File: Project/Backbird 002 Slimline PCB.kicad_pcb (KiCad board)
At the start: 2 copper layers, 10 parts

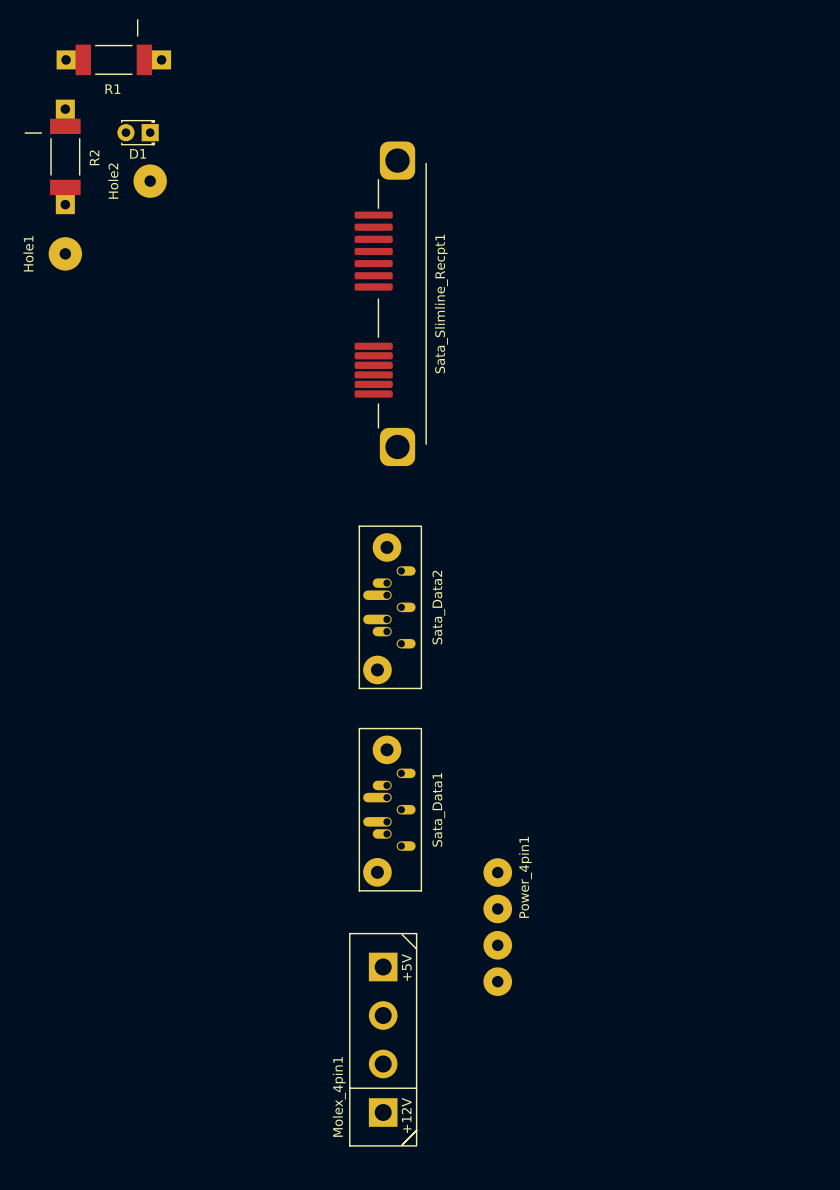
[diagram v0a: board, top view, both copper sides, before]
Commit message: Updated PSB layout. (might remove extra power and Sata locations) Added custom footprints for screws and for a generic 8981 power pinout.
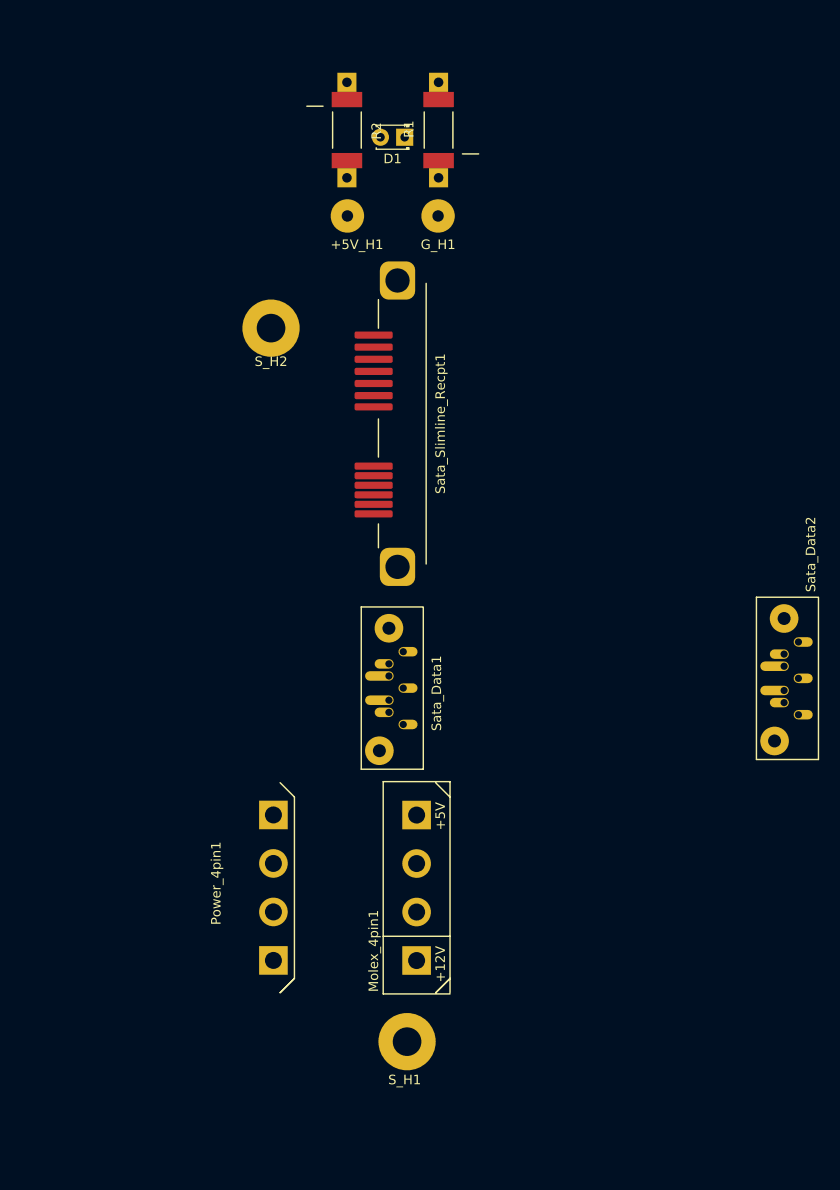
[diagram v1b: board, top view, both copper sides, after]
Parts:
- removed Hole1, Hole2: Conn_01x01, Wire_Pads:SolderWirePad_single_1-2mmDrill
- added +5V_H1: Conn_01x01, Wire_Pads:SolderWirePad_single_1-2mmDrill, F.Cu at (102.5, 46.5)
- added G_H1: Conn_01x01, Wire_Pads:SolderWirePad_single_1-2mmDrill, F.Cu at (112.0, 46.5)
- added S_H1: Conn_01x01, ProjectFootprints:Blackbird002_Slimline_PCB_Screw, F.Cu at (108.8, 133.0)
- added S_H2: Conn_01x01, ProjectFootprints:Blackbird002_Slimline_PCB_Screw, F.Cu at (94.5, 58.2)
- Power_4pin1: footprint Wire_Pads:SolderWirePad_4xInline_1-2mmDrill -> ProjectFootprints:MOLEX_8981_Generic
- moved Sata_Data2 42.3 mm to (152.7, 103.3)
- moved R1 34.8 mm to (112.1, 37.5), turned to 90 degrees
- moved R2 29.6 mm to (102.5, 37.5)
- moved D1 26.7 mm to (108.5, 38.2)
- moved Power_4pin1 23.9 mm to (94.8, 116.8)
- moved Molex_4pin1 16.3 mm to (109.8, 116.9)
- moved Sata_Data1 12.7 mm to (111.3, 104.3)
- moved Sata_Slimline_Recpt1 12.6 mm to (107.8, 68.2)

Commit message: Removed extra connectors from PCB
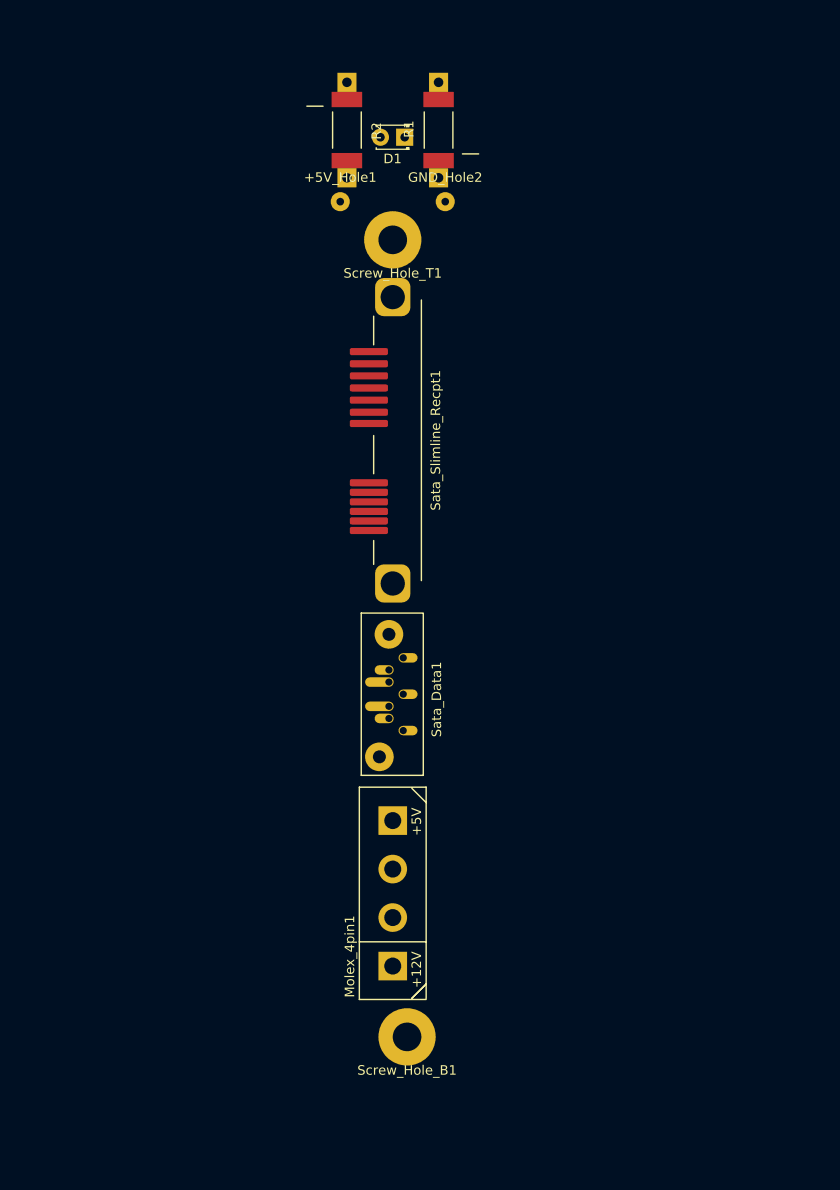
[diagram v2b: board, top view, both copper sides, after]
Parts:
- removed +5V_H1, G_H1: Conn_01x01, Wire_Pads:SolderWirePad_single_1-2mmDrill
- removed Power_4pin1: Conn_01x04, ProjectFootprints:MOLEX_8981_Generic
- removed S_H1, S_H2: Conn_01x01, ProjectFootprints:Blackbird002_Slimline_PCB_Screw
- removed Sata_Data2: Conn_01x07, ProjectFootprints:SATA_DATA_678007005_CustomPad
- added +5V_Hole1: Conn_01x01, Wire_Pads:SolderWirePad_single_0-8mmDrill, F.Cu at (101.8, 45.0)
- added GND_Hole2: Conn_01x01, Wire_Pads:SolderWirePad_single_0-8mmDrill, F.Cu at (112.8, 45.0)
- added Screw_Hole_B1: Conn_01x01, ProjectFootprints:Blackbird002_Slimline_PCB_Screw, F.Cu at (108.8, 132.5)
- added Screw_Hole_T1: Conn_01x01, ProjectFootprints:Blackbird002_Slimline_PCB_Screw, F.Cu at (107.3, 49.0)
- moved Molex_4pin1 2.57 mm to (107.3, 117.4)
- moved Sata_Slimline_Recpt1 1.81 mm to (107.3, 70.0)
- moved Sata_Data1 0.64 mm to (111.3, 105.0)
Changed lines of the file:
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@@
     (tracks 0)
     (zones 0)
-    (modules 12)
+    (modules 10)
     (nets 13)
   )
@@
   )
   (module ProjectFootprints:SATA_DATA_678007005_CustomPad (layer F.Cu)
-    (at 111.3 104.34 90)
+    (at 111.3 104.98 90)
     (fp_text reference Sata_Data1 (at 7.86 0.6 90) (layer F.SilkS)
       (effects (font (size 1 1) (thickness 0.15)))
@@
   )
   (module ProjectFootprints:MOLEX_8981_0015244745 (layer F.Cu)
-    (at 109.8 116.86 90)
+    (at 107.3 117.44 90)
     (fp_text reference Molex_4pin1 (at -6.62 -4.5 90) (layer F.SilkS)
       (effects (font (size 1 1) (thickness 0.15)))
@@
       (net 1 "Net-(D1-Pad2)"))
   )
-  (module ProjectFootprints:SATA_DATA_678007005_CustomPad (layer F.Cu)
-    (at 152.7 103.32 90)
-    (fp_text reference Sata_Data2 (at 21.39 -1.6 90) (layer F.SilkS)
-      (effects (font (size 1 1) (thickness 0.15)))
-    )
-    (fp_text value Conn_01x07 (at 8.4 -9.504 90) (layer F.Fab)
-      (effects (font (size 1 1) (thickness 0.15)))
-    )
-    (fp_line (start 16.9 -7.3) (end 16.9 -0.9) (layer F.SilkS) (width 0.15))
-    (fp_line (start -0.1 -7.3) (end 16.9 -7.3) (layer F.SilkS) (width 0.15))
-    (fp_line (start -0.1 -0.8) (end -0.1 -7.3) (layer F.SilkS) (width 0.15))
-    (fp_line (start -0.1 -0.8) (end 16.9 -0.8) (layer F.SilkS) (width 0.15))
-    (pad 1 thru_hole oval (at 12.21 -2.9 270) (size 1 2) (drill 0.75 (offset 0 -0.5)) (layers *.Cu *.Mask)
-      (net 2 GND))
-    (pad 4 thru_hole oval (at 8.4 -2.9 270) (size 1 2) (drill 0.75 (offset 0 -0.5)) (layers *.Cu *.Mask)
-      (net 2 GND))
-    (pad 7 thru_hole oval (at 4.59 -2.9 270) (size 1 2) (drill 0.75 (offset 0 -0.5)) (layers *.Cu *.Mask)
-      (net 2 GND))
-    (pad 2 thru_hole oval (at 10.94 -4.4 90) (size 1 2) (drill 0.75 (offset 0 -0.5)) (layers *.Cu *.Mask)
-      (net 8 A+))
-    (pad 3 thru_hole oval (at 9.67 -4.4 90) (size 1 3) (drill 0.75 (offset 0 -1)) (layers *.Cu *.Mask)
-      (net 7 A-))
-    (pad 5 thru_hole oval (at 7.13 -4.4 90) (size 1 3) (drill 0.75 (offset 0 -1)) (layers *.Cu *.Mask)
-      (net 6 B-))
-    (pad 8 thru_hole circle (at 1.84 -5.4 90) (size 3 3) (drill 1.36) (layers *.Cu *.Mask))
-    (pad 8 thru_hole circle (at 14.67 -4.4 90) (size 3 3) (drill 1.36) (layers *.Cu *.Mask))
-    (pad 6 thru_hole oval (at 5.86 -4.4 90) (size 1 2) (drill 0.75 (offset 0 -0.5)) (layers *.Cu *.Mask)
-      (net 5 B+))
-  )
   (module ProjectFootprints:SATA_SLIMLINE_RECPT_1735539-2 (layer F.Cu)
-    (at 107.8 68.24 90)
+    (at 107.3 69.98 90)
     (attr smd)
     (fp_text reference Sata_Slimline_Recpt1 (at 0 4.5 90) (layer F.SilkS)
@@
       (net 2 GND))
   )
-  (module Wire_Pads:SolderWirePad_single_1-2mmDrill (layer F.Cu)
-    (at 102.55 46.4792)
-    (fp_text reference +5V_H1 (at 1 3.0008) (layer F.SilkS)
-      (effects (font (size 1 1) (thickness 0.15)))
-    )
-    (fp_text value Conn_01x01 (at -8.5 0.5008) (layer F.Fab)
-      (effects (font (size 1 1) (thickness 0.15)))
-    )
-    (pad 1 thru_hole circle (at 0 0) (size 3.50012 3.50012) (drill 1.19888) (layers *.Cu *.Mask)
-      (net 3 +5V))
-  )
-  (module Wire_Pads:SolderWirePad_single_1-2mmDrill (layer F.Cu)
-    (at 112.05 46.48)
-    (fp_text reference G_H1 (at 0 3) (layer F.SilkS)
-      (effects (font (size 1 1) (thickness 0.15)))
-    )
-    (fp_text value Conn_01x01 (at 7.5 0.25) (layer F.Fab)
-      (effects (font (size 1 1) (thickness 0.15)))
-    )
-    (pad 1 thru_hole circle (at 0 0) (size 3.50012 3.50012) (drill 1.19888) (layers *.Cu *.Mask)
-      (net 2 GND))
-  )
   (module ProjectFootprints:Blackbird002_Slimline_PCB_Screw (layer F.Cu)
-    (at 108.8 132.98)
-    (fp_text reference S_H1 (at -0.25 4) (layer F.SilkS)
+    (at 108.8 132.48)
+    (fp_text reference Screw_Hole_B1 (at 0 3.5) (layer F.SilkS)
       (effects (font (size 1 1) (thickness 0.15)))
     )
@@
   )
   (module ProjectFootprints:Blackbird002_Slimline_PCB_Screw (layer F.Cu)
-    (at 94.55 58.23)
-    (fp_text reference S_H2 (at 0 3.5) (layer F.SilkS)
+    (at 107.3 48.98)
+    (fp_text reference Screw_Hole_T1 (at 0 3.5) (layer F.SilkS)
       (effects (font (size 1 1) (thickness 0.15)))
     )
@@
       (net 12 "Net-(Screw_Hole_T1-Pad1)"))
   )
-  (module ProjectFootprints:MOLEX_8981_Generic (layer F.Cu)
-    (at 94.8 116.85 90)
-    (fp_text reference Power_4pin1 (at 0.46 -6 90) (layer F.SilkS)
-      (effects (font (size 1 1) (thickness 0.15)))
-    )
-    (fp_text value Conn_01x04 (at 0 -4.5 90) (layer F.Fab)
-      (effects (font (size 1 1) (thickness 0.15)))
-    )
-    (fp_line (start -11.25 -3.65) (end 11.25 -3.65) (layer F.CrtYd) (width 0.05))
-    (fp_line (start -9.5 2.2) (end -11 0.7) (layer F.SilkS) (width 0.15))
-    (fp_line (start -11 0.7) (end -9.5 2.2) (layer F.SilkS) (width 0.15))
-    (fp_line (start 9.5 2.2) (end 11 0.7) (layer F.SilkS) (width 0.15))
-    (fp_line (start 9.5 2.2) (end -9.5 2.2) (layer F.SilkS) (width 0.15))
-    (pad 1 thru_hole rect (at -7.62 0 90) (size 3 3) (drill 1.78) (layers *.Cu *.Mask)
-      (net 4 +12V))
-    (pad 2 thru_hole circle (at -2.54 0 90) (size 3 3) (drill 1.78) (layers *.Cu *.Mask)
-      (net 2 GND))
-    (pad 3 thru_hole circle (at 2.54 0 90) (size 3 3) (drill 1.78) (layers *.Cu *.Mask)
-      (net 2 GND))
-    (pad 4 thru_hole rect (at 7.62 0 90) (size 3 3) (drill 1.78) (layers *.Cu *.Mask)
-      (net 3 +5V))
+  (module Wire_Pads:SolderWirePad_single_0-8mmDrill (layer F.Cu)
+    (at 101.8 44.98)
+    (fp_text reference +5V_Hole1 (at 0 -2.54) (layer F.SilkS)
+      (effects (font (size 1 1) (thickness 0.15)))
+    )
+    (fp_text value Conn_01x01 (at 0 2.54) (layer F.Fab)
+      (effects (font (size 1 1) (thickness 0.15)))
+    )
+    (pad 1 thru_hole circle (at 0 0) (size 1.99898 1.99898) (drill 0.8001) (layers *.Cu *.Mask)
+      (net 3 +5V))
+  )
+  (module Wire_Pads:SolderWirePad_single_0-8mmDrill (layer F.Cu)
+    (at 112.8 44.98)
+    (fp_text reference GND_Hole2 (at 0 -2.54) (layer F.SilkS)
+      (effects (font (size 1 1) (thickness 0.15)))
+    )
+    (fp_text value Conn_01x01 (at 0 2.54) (layer F.Fab)
+      (effects (font (size 1 1) (thickness 0.15)))
+    )
+    (pad 1 thru_hole circle (at 0 0) (size 1.99898 1.99898) (drill 0.8001) (layers *.Cu *.Mask)
+      (net 2 GND))
   )
   (dimension 8 (width 0.3) (layer Eco1.User)
